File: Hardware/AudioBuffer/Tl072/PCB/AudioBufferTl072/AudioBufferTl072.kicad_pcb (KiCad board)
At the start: 2 copper layers, 34 parts, among them J1 Conn_01x06_Male, J2 Conn_01x02_Pin, J3 Conn_01x06_Male, J4 Conn_01x02_Pin, J5 AudioJack3, J6 AudioJack3, U1 TL072, U2 TL072

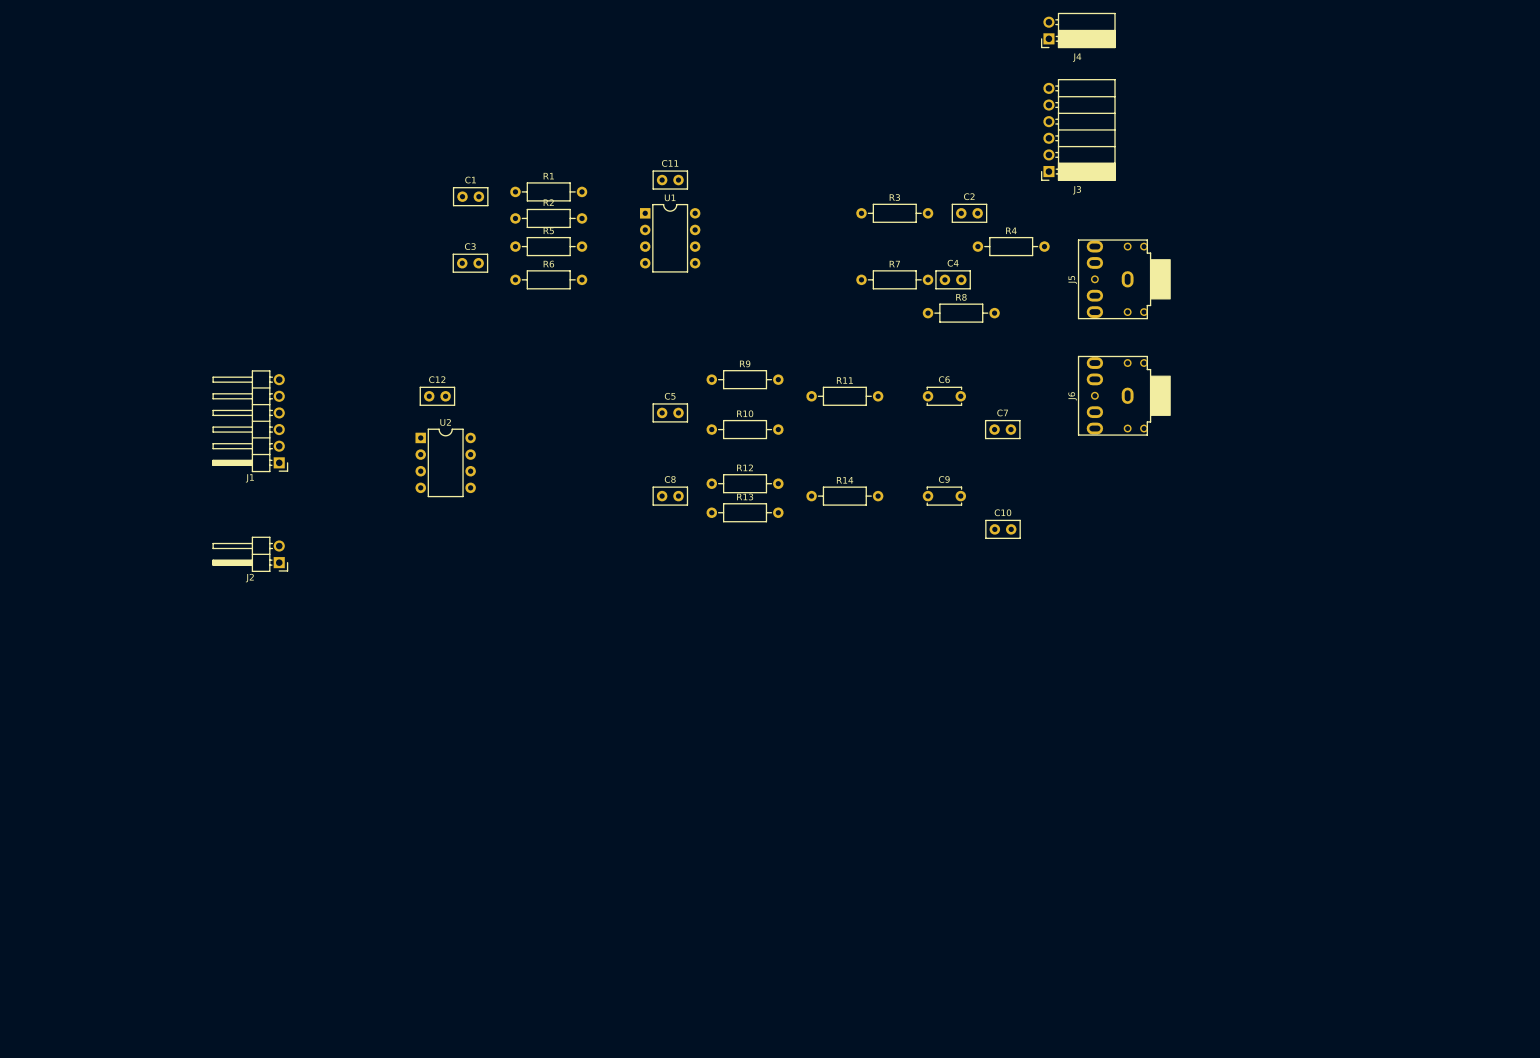
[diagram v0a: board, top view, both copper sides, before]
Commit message: Updates to audio buffer
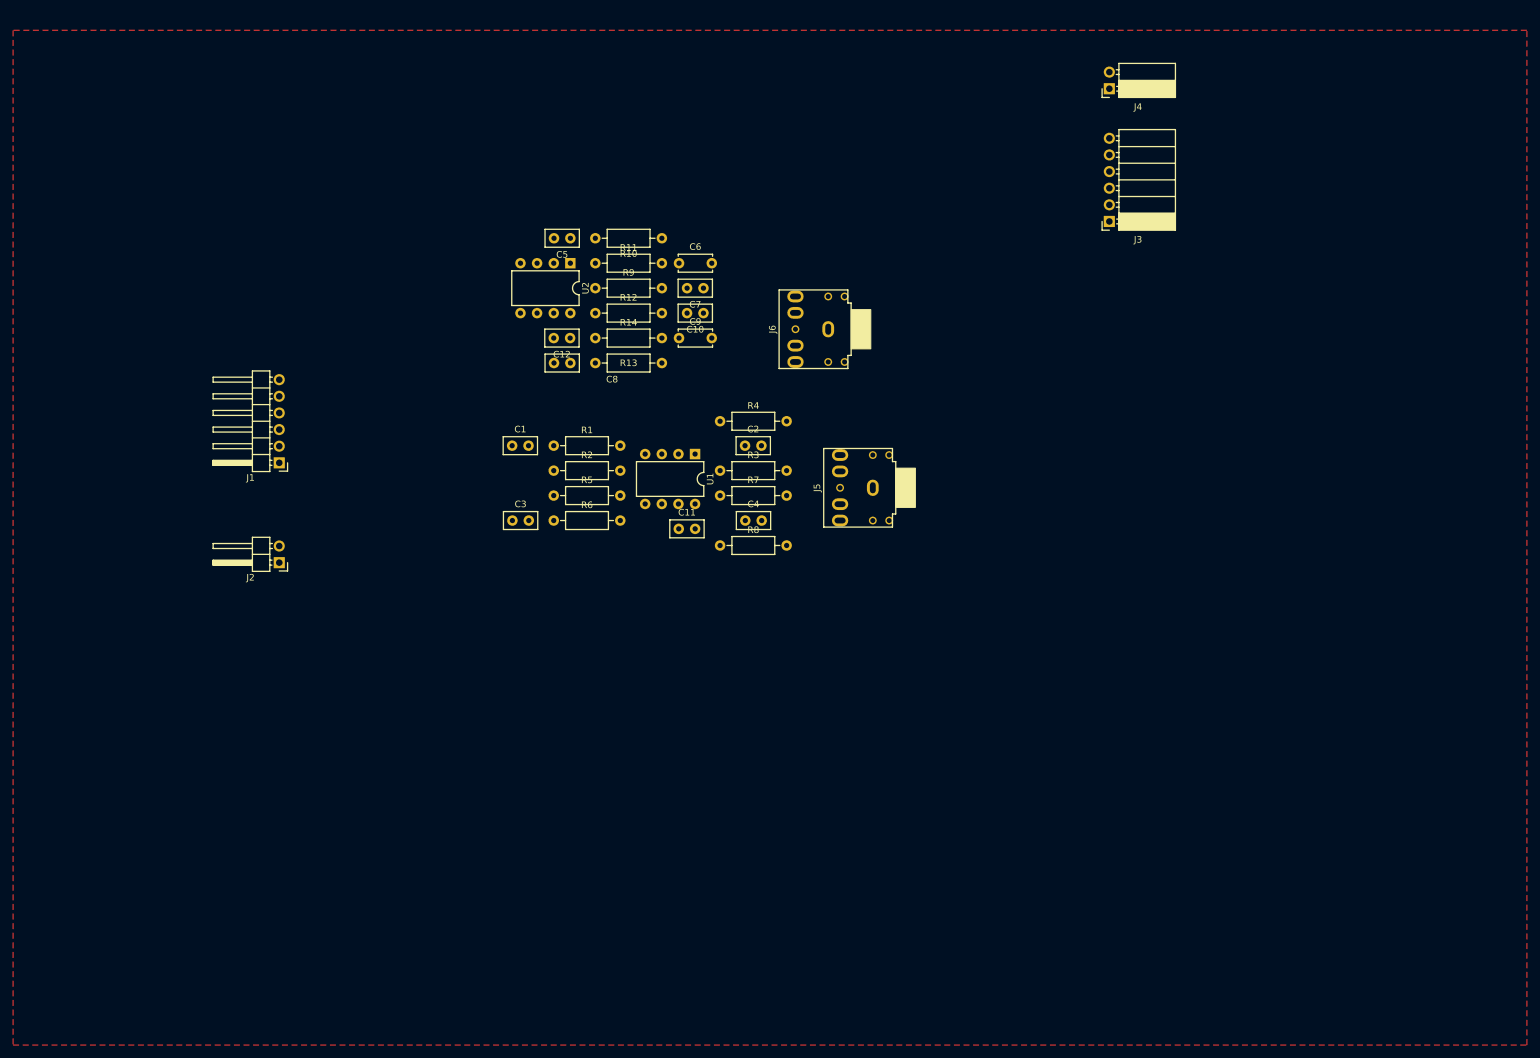
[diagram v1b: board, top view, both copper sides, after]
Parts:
- moved C10 55.4 mm to (156.2, 66.0), turned to 180 degrees
- moved C11 53.3 mm to (152.4, 99.0)
- moved J5 50.3 mm to (179.1, 92.7)
- moved C7 49.4 mm to (156.2, 62.2), turned to 180 degrees
- moved C2 48.5 mm to (162.6, 86.3)
- moved C4 47.7 mm to (162.6, 97.7)
- moved R8 47.6 mm to (158.8, 101.5)
- moved R4 47.6 mm to (158.8, 82.5)
- moved J6 46.8 mm to (172.3, 68.5)
- moved C9 45.0 mm to (152.5, 69.8)
- moved R3 44.8 mm to (158.8, 90.1)
- moved C6 43.1 mm to (152.5, 58.4)
- moved R14 40.9 mm to (139.7, 69.8)
- moved C3 40.0 mm to (127.0, 97.7)
- moved R7 39.4 mm to (158.8, 93.9)
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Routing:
- added copper zone on F.Cu, net GND

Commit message: Isolator added
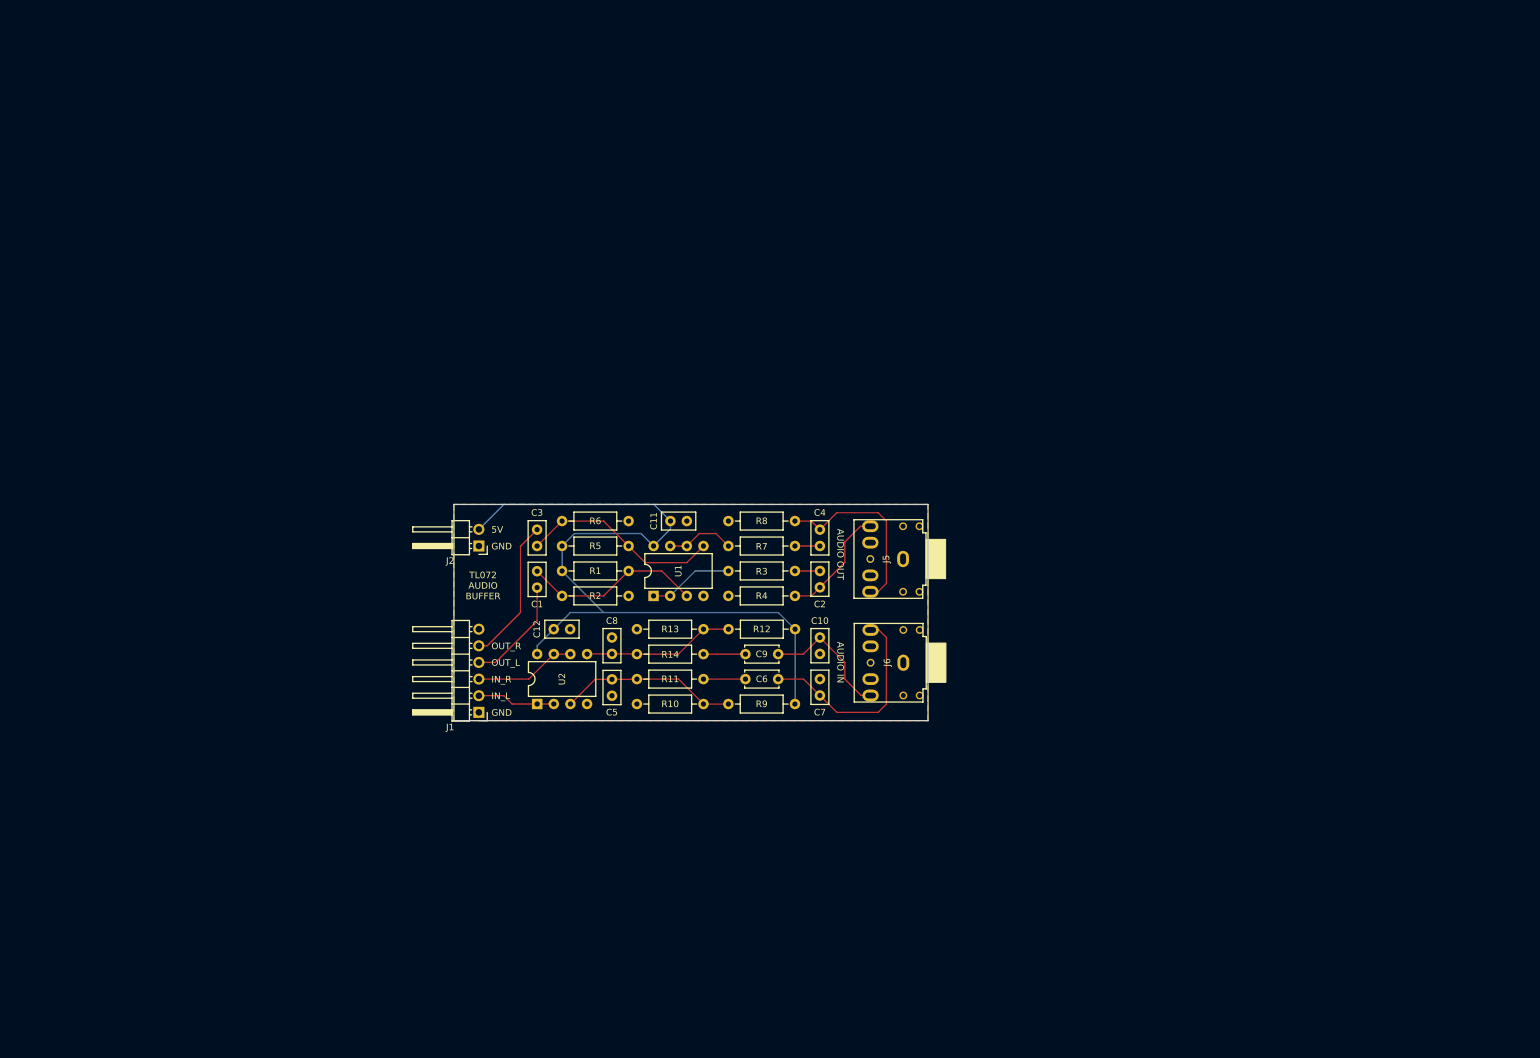
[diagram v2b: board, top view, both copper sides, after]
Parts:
- removed J3: Conn_01x06_Male, Connector_PinSocket_2.54mm:PinSocket_1x06_P2.54mm_Horizontal
- removed J4: Conn_01x02_Pin, Connector_PinSocket_2.54mm:PinSocket_1x02_P2.54mm_Horizontal
- moved R10 71.2 mm to (146.1, 125.7), turned to 0 degrees
- moved C5 67.6 mm to (142.2, 122.0), turned to -90 degrees
- moved U2 67.5 mm to (130.8, 125.7), turned to 90 degrees
- moved R9 66.7 mm to (160.0, 125.7)
- moved C7 64.7 mm to (174.0, 124.4), turned to 90 degrees
- moved C6 64.3 mm to (162.6, 121.9)
- moved R11 63.8 mm to (146.1, 121.9)
- moved C10 52.6 mm to (174.0, 115.6), turned to -90 degrees
- moved R12 52.4 mm to (160.0, 114.3)
- moved J6 52.2 mm to (183.7, 119.4)
- moved C9 49.3 mm to (162.6, 118.1)
- moved J1 48.8 mm to (121.9, 127.0)
- moved R14 48.7 mm to (146.1, 118.1)
- moved C8 44.9 mm to (142.2, 118.1), turned to 90 degrees
- moved C12 44.5 mm to (133.3, 114.3), turned to 0 degrees
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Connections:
- J1 pad 2: AUDIO_OUT_R -> AUDIO_IN_L
- J1 pad 3: AUDIO_OUT_L -> AUDIO_IN_R
- J1 pad 4: AUDIO_IN_R -> AUDIO_OUT_L
- J1 pad 5: AUDIO_IN_L -> AUDIO_OUT_R
- J1 pad 6: GND -> NC
- J2 pad 1: 5V -> GND
- J2 pad 2: GND -> 5V
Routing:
- net 5V: track 0.00 -> 120.3 mm
- net EXT_AUDIO_IN_L: track 0.00 -> 32.2 mm
- net Net-(U1B-+): track 0.00 -> 30.7 mm
- net EXT_AUDIO_OUT_R: track 0.00 -> 28.6 mm
- net Net-(U1A-+): track 0.00 -> 27.6 mm
- net Net-(U2A-+): track 0.00 -> 27.3 mm
- net Net-(U2B-+): track 0.00 -> 23.2 mm
- net AUDIO_OUT_R: track 0.00 -> 22.2 mm
- net EXT_AUDIO_IN_R: track 0.00 -> 20.3 mm
- net EXT_AUDIO_OUT_L: track 0.00 -> 17.1 mm
- net AUDIO_OUT_L: track 0.00 -> 16.6 mm
- net AUDIO_IN_R: track 0.00 -> 15.6 mm
- net Net-(U1A--): track 0.00 -> 13.0 mm
- net AUDIO_IN_L: track 0.00 -> 12.0 mm
- net Net-(U1B--): track 0.00 -> 10.5 mm
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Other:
- board outline added: 72.4 x 33 mm
- board text added: "5V"
- board text added: "AUDIO IN"
- board text added: "AUDIO OUT"
- board text added: "GND"
- board text added: "IN_L"
- board text added: "IN_R"
- board text added: "OUT_L"
- board text added: "OUT_R"
- board text added: "TL072 AUDIO BUFFER"
